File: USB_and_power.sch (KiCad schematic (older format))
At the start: 38 parts

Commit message: Updated with the ttl output
Adding a lot of footprints and other bits.
Changed TVS on USB
Added fuse on USB 5V
TTL level translators, 2x. Go from 3v3 to 1v8, then "anything" to 1v8
for the output.
2x LDO for 3v3->1v8, 3v3->2v5
Plus allow external input.
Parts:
- removed D? (x2): D_TVS, symbol Device:D_TVS
- added D1: RClamp0582BQ, Package_TO_SOT_SMD:SOT-416, symbol Power_Protection:SP0502BAJT
- added F1: 0ZCJ0075AF2E, Resistor_SMD:R_1206_3216Metric_Pad1.30x1.75mm_HandSolder, symbol Device:Polyfuse_Small
- C1, C10, C11, C12, C13, C14, C15, C16, C17, C18, C4, C5, C6, C7, C8, C9: renamed from C?; footprint (none) -> Capacitor_SMD:C_0603_1608Metric_Pad1.08x0.95mm_HandSolder
- C2: renamed from C?; footprint (none) -> Capacitor_Tantalum_SMD:CP_EIA-3528-21_Kemet-B_Pad1.50x2.35mm_HandSolder
- C3: renamed from C?; footprint (none) -> Capacitor_SMD:CP_Elec_6.3x5.7
- D3: renamed from D?; value MBRS140 -> 1A 20V; footprint (none) -> Diode_SMD:D_SOD-123
- J1: renamed from J?; footprint (none) -> Connector_USB:USB_Micro-AB_Molex_47590-0001
- R1: renamed from R?; footprint (none) -> Resistor_SMD:R_0603_1608Metric_Pad0.98x0.95mm_HandSolder
- R2, R3, R4, R5, R6, R7, R8: renamed from R?; footprint (none) -> Connector_PinHeader_2.00mm:PinHeader_1x02_P2.00mm_Vertical_SMD_Pin1Left
- U2: renamed from U?; footprint (none) -> Package_SO:SO-8_3.9x4.9mm_P1.27mm
- U3: renamed from U?; footprint (none) -> Package_QFP:LQFP-64_10x10mm_P0.5mm
- Y1: renamed from Y?; footprint (none) -> Crystal:Crystal_SMD_HC49-SD_HandSoldering
- gave numbers to parts that had none: 5
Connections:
- wire segments 213 -> 215
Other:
- note added: "750mA Bel Fuse"

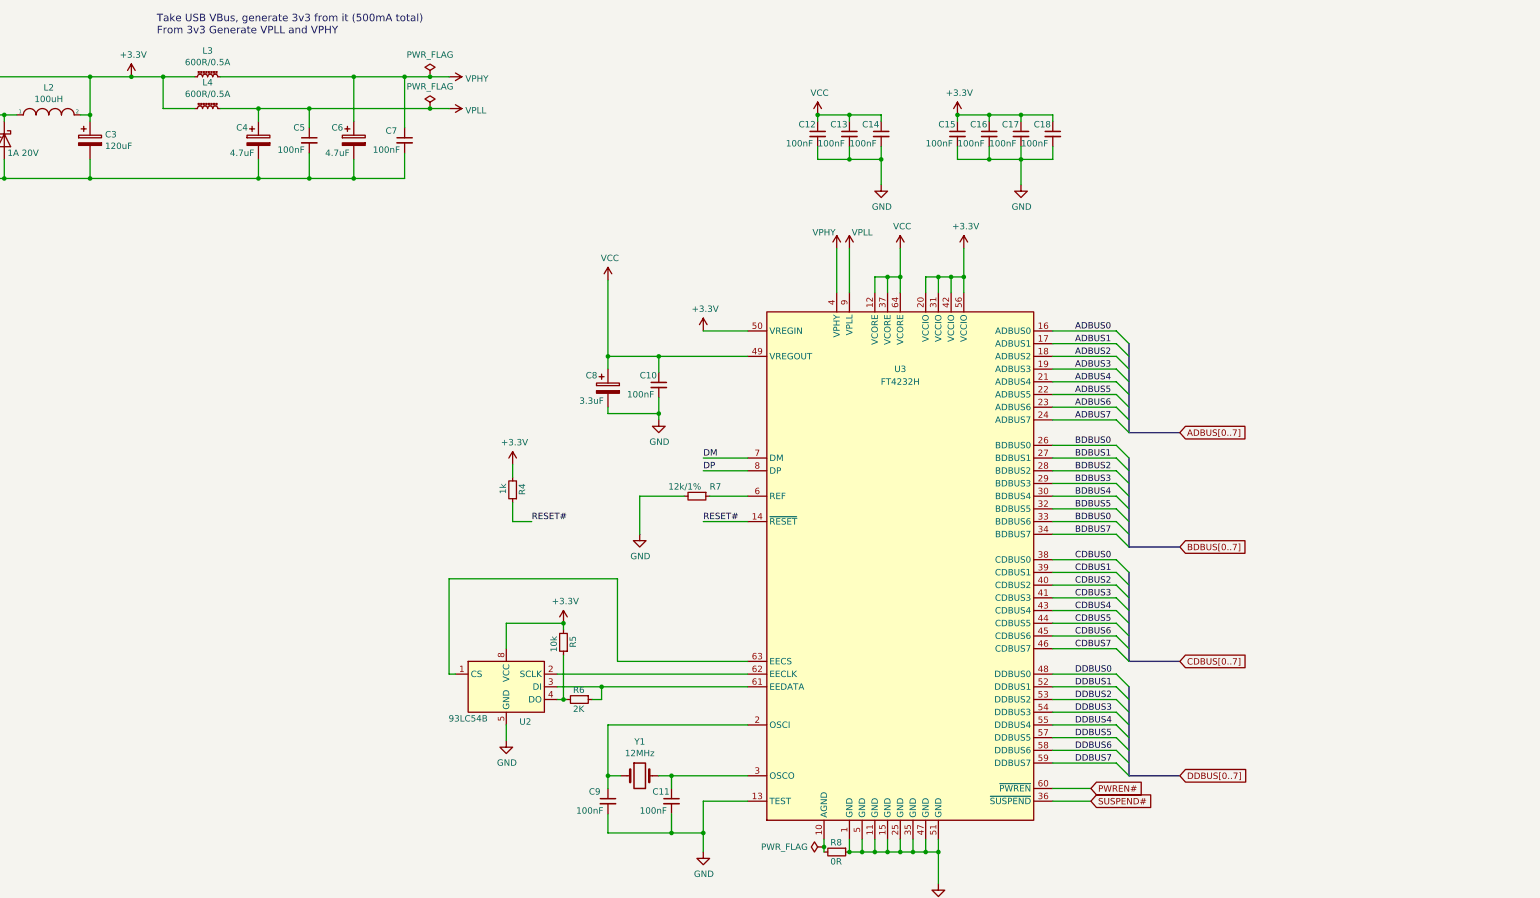
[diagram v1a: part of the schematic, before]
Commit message: Adding some LED stuff.
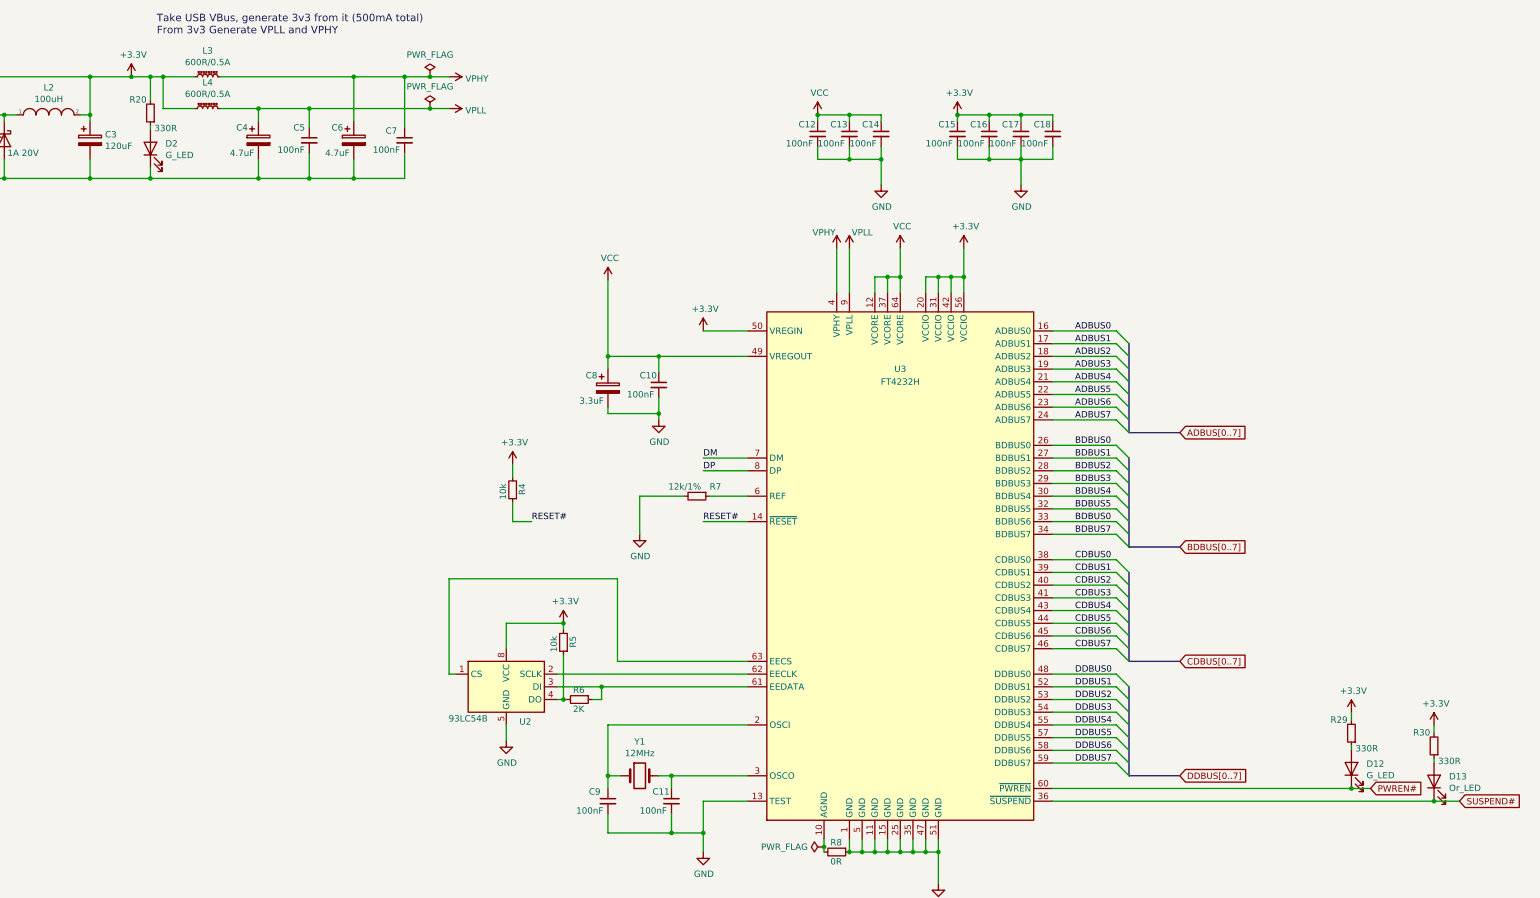
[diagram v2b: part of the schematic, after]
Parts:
- added D12, D2: G_LED, LED_SMD:LED_0603_1608Metric_Pad1.05x0.95mm_HandSolder, symbol Device:LED
- added D13: Or_LED, LED_SMD:LED_0603_1608Metric_Pad1.05x0.95mm_HandSolder, symbol Device:LED
- added R20, R29, R30: 330R, Resistor_SMD:R_0603_1608Metric_Pad0.98x0.95mm_HandSolder, symbol Device:R_Small
- R2, R3, R5, R6, R7, R8: footprint Connector_PinHeader_2.00mm:PinHeader_1x02_P2.00mm_Vertical_SMD_Pin1Left -> Resistor_SMD:R_0603_1608Metric_Pad0.98x0.95mm_HandSolder
- R4: value 1k -> 10k; footprint Connector_PinHeader_2.00mm:PinHeader_1x02_P2.00mm_Vertical_SMD_Pin1Left -> Resistor_SMD:R_0603_1608Metric_Pad0.98x0.95mm_HandSolder
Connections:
- net +3V3: now also R20.2, R29.2, R30.2
- net GND: now also D2.1 (K)
- net PWREN#: now also D12.1 (K)
- net SUSPEND#: now also D13.1 (K)
- new net: D2.2 (A), R20.1
- new net: D13.2 (A), R30.1
- new net: D12.2 (A), R29.1
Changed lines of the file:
@@
 F 0 "R2" V 3025 4900 50  0000 L CNN
 F 1 "10R" V 3025 4575 50  0000 L CNN
-F 2 "Connector_PinHeader_2.00mm:PinHeader_1x02_P2.00mm_Vertical_SMD_Pin1Left" H 3100 4800 50  0001 C CNN
+F 2 "Resistor_SMD:R_0603_1608Metric_Pad0.98x0.95mm_HandSolder" H 3100 4800 50  0001 C CNN
 F 3 "~" H 3100 4800 50  0001 C CNN
 	1    3100 4800
@@
 F 0 "R3" V 3175 5000 50  0000 L CNN
 F 1 "R10" V 3175 4675 50  0000 L CNN
-F 2 "Connector_PinHeader_2.00mm:PinHeader_1x02_P2.00mm_Vertical_SMD_Pin1Left" H 3100 4900 50  0001 C CNN
+F 2 "Resistor_SMD:R_0603_1608Metric_Pad0.98x0.95mm_HandSolder" H 3100 4900 50  0001 C CNN
 F 3 "~" H 3100 4900 50  0001 C CNN
 	1    3100 4900
@@
 	5250 3150 5500 3150
 Wire Wire Line
-	5250 3150 5000 3150
+	5250 3150 5150 3150
 Connection ~ 5000 3150
 Connection ~ 5250 3150
@@
 $EndComp
 Wire Wire Line
-	4675 3950 6000 3950
+	4675 3950 5150 3950
 Wire Wire Line
 	6000 3950 6000 3800
@@
 F 0 "R7" V 9375 6550 50  0000 L CNN
 F 1 "12k/1%" V 9375 6225 50  0000 L CNN
-F 2 "Connector_PinHeader_2.00mm:PinHeader_1x02_P2.00mm_Vertical_SMD_Pin1Left" H 9450 6450 50  0001 C CNN
+F 2 "Resistor_SMD:R_0603_1608Metric_Pad0.98x0.95mm_HandSolder" H 9450 6450 50  0001 C CNN
 F 3 "~" H 9450 6450 50  0001 C CNN
 	1    9450 6450
@@
 F 0 "R8" V 10475 9200 50  0000 L CNN
 F 1 "0R" V 10625 9200 50  0000 L CNN
-F 2 "Connector_PinHeader_2.00mm:PinHeader_1x02_P2.00mm_Vertical_SMD_Pin1Left" H 10550 9250 50  0001 C CNN
+F 2 "Resistor_SMD:R_0603_1608Metric_Pad0.98x0.95mm_HandSolder" H 10550 9250 50  0001 C CNN
 F 3 "~" H 10550 9250 50  0001 C CNN
 	1    10550 9250
@@
 F 0 "R6" V 8450 8000 50  0000 L CNN
 F 1 "2K" V 8600 8000 50  0000 L CNN
-F 2 "Connector_PinHeader_2.00mm:PinHeader_1x02_P2.00mm_Vertical_SMD_Pin1Left" H 8525 8050 50  0001 C CNN
+F 2 "Resistor_SMD:R_0603_1608Metric_Pad0.98x0.95mm_HandSolder" H 8525 8050 50  0001 C CNN
 F 3 "~" H 8525 8050 50  0001 C CNN
 	1    8525 8050
@@
 F 0 "R5" V 8325 7550 50  0000 L CNN
 F 1 "10k" V 8475 7550 50  0000 L CNN
-F 2 "Connector_PinHeader_2.00mm:PinHeader_1x02_P2.00mm_Vertical_SMD_Pin1Left" H 8400 7600 50  0001 C CNN
+F 2 "Resistor_SMD:R_0603_1608Metric_Pad0.98x0.95mm_HandSolder" H 8400 7600 50  0001 C CNN
 F 3 "~" H 8400 7600 50  0001 C CNN
 	1    8400 7600
@@
 P 8000 6400
 F 0 "R4" V 7925 6350 50  0000 L CNN
-F 1 "1k" V 8075 6350 50  0000 L CNN
-F 2 "Connector_PinHeader_2.00mm:PinHeader_1x02_P2.00mm_Vertical_SMD_Pin1Left" H 8000 6400 50  0001 C CNN
+F 1 "10k" V 8075 6350 50  0000 L CNN
+F 2 "Resistor_SMD:R_0603_1608Metric_Pad0.98x0.95mm_HandSolder" H 8000 6400 50  0001 C CNN
 F 3 "~" H 8000 6400 50  0001 C CNN
 	1    8000 6400
@@
 	8000 6200 8000 6300
 Wire Wire Line
-	12250 8750 12550 8750
-Wire Wire Line
-	12250 8850 12550 8850
-Text GLabel 12550 8750 2    50   Input ~ 0
+	12250 8750 14600 8750
+Text GLabel 14750 8750 2    50   Input ~ 0
 PWREN#
-Text GLabel 12550 8850 2    50   Input ~ 0
+Text GLabel 15450 8850 2    50   Input ~ 0
 SUSPEND#
 $Comp
@@
 Wire Wire Line
 	2100 5500 2100 5400
+Text Notes 810  4175 0    50   ~ 0
+750mA Bel Fuse
+Wire Wire Line
+	5150 3565 5150 3535
+Connection ~ 5150 3150
+Wire Wire Line
+	5150 3150 5000 3150
+Wire Wire Line
+	5150 3865 5150 3950
+Connection ~ 5150 3950
+Wire Wire Line
+	5150 3950 6000 3950
+$Comp
+L Device:R_Small R20
+U 1 1 614A5B2C
+P 5150 3435
+F 0 "R20" H 5180 3330 50  0000 L CNN
+F 1 "330R" H 4940 3555 50  0000 L CNN
+F 2 "Resistor_SMD:R_0603_1608Metric_Pad0.98x0.95mm_HandSolder" H 5150 3435 50  0001 C CNN
+F 3 "~" H 5150 3435 50  0001 C CNN
+	1    5150 3435
+	-1   0    0    1
+$EndComp
+Wire Wire Line
+	5150 3335 5150 3150
+$Comp
+L Device:LED D2
+U 1 1 61481FAA
+P 5150 3715
+F 0 "D2" V 5189 3597 50  0000 R CNN
+F 1 "G_LED" V 5098 3597 50  0000 R CNN
+F 2 "LED_SMD:LED_0603_1608Metric_Pad1.05x0.95mm_HandSolder" H 5150 3715 50  0001 C CNN
+F 3 "~" H 5150 3715 50  0001 C CNN
+	1    5150 3715
+	0    -1   -1   0
+$EndComp
+Wire Wire Line
+	15250 8545 15250 8515
+$Comp
+L Device:R_Small R30
+U 1 1 61840081
+P 15250 8415
+F 0 "R30" H 15280 8310 50  0000 L CNN
+F 1 "330R" H 15040 8535 50  0000 L CNN
+F 2 "Resistor_SMD:R_0603_1608Metric_Pad0.98x0.95mm_HandSolder" H 15250 8415 50  0001 C CNN
+F 3 "~" H 15250 8415 50  0001 C CNN
+	1    15250 8415
+	-1   0    0    1
+$EndComp
+$Comp
+L Device:LED D13
+U 1 1 6184008B
+P 15250 8695
+F 0 "D13" V 15289 8577 50  0000 R CNN
+F 1 "Or_LED" V 15198 8577 50  0000 R CNN
+F 2 "LED_SMD:LED_0603_1608Metric_Pad1.05x0.95mm_HandSolder" H 15250 8695 50  0001 C CNN
+F 3 "~" H 15250 8695 50  0001 C CNN
+	1    15250 8695
+	0    -1   -1   0
+$EndComp
+$Comp
+L power:+3.3V #PWR04
+U 1 1 61872E5E
+P 15250 8255
+F 0 "#PWR04" H 15250 8105 50  0001 C CNN
+F 1 "+3.3V" H 15265 8428 50  0000 C CNN
+F 2 "" H 15250 8255 50  0001 C CNN
+F 3 "" H 15250 8255 50  0001 C CNN
+	1    15250 8255
+	1    0    0    -1
+$EndComp
+Wire Wire Line
+	15250 8255 15250 8315
+Wire Wire Line
+	12250 8850 15250 8850
+Wire Wire Line
+	14600 8445 14600 8415
+$Comp
+L Device:R_Small R29
+U 1 1 618CACEF
+P 14600 8315
+F 0 "R29" H 14630 8210 50  0000 L CNN
+F 1 "330R" H 14390 8435 50  0000 L CNN
+F 2 "Resistor_SMD:R_0603_1608Metric_Pad0.98x0.95mm_HandSolder" H 14600 8315 50  0001 C CNN
+F 3 "~" H 14600 8315 50  0001 C CNN
+	1    14600 8315
+	-1   0    0    1
+$EndComp
+$Comp
+L Device:LED D12
+U 1 1 618CACF9
+P 14600 8595
+F 0 "D12" V 14639 8477 50  0000 R CNN
+F 1 "G_LED" V 14548 8477 50  0000 R CNN
+F 2 "LED_SMD:LED_0603_1608Metric_Pad1.05x0.95mm_HandSolder" H 14600 8595 50  0001 C CNN
+F 3 "~" H 14600 8595 50  0001 C CNN
+	1    14600 8595
+	0    -1   -1   0
+$EndComp
+$Comp
+L power:+3.3V #PWR03
+U 1 1 618CAD03
+P 14600 8155
+F 0 "#PWR03" H 14600 8005 50  0001 C CNN
+F 1 "+3.3V" H 14615 8328 50  0000 C CNN
+F 2 "" H 14600 8155 50  0001 C CNN
+F 3 "" H 14600 8155 50  0001 C CNN
+	1    14600 8155
+	1    0    0    -1
+$EndComp
+Wire Wire Line
+	14600 8155 14600 8215
+Wire Wire Line
+	14600 8750 14600 8745
+Connection ~ 14600 8750
+Wire Wire Line
+	14600 8750 14750 8750
+Wire Wire Line
+	15250 8850 15250 8845
 Wire Bus Line
 	12850 5250 12850 5950
@@
 Wire Bus Line
 	12850 7950 12850 8650
-Text Notes 810  4175 0    50   ~ 0
-750mA Bel Fuse
+Connection ~ 15250 8850
+Wire Wire Line
+	15250 8850 15450 8850
 $EndSCHEMATC

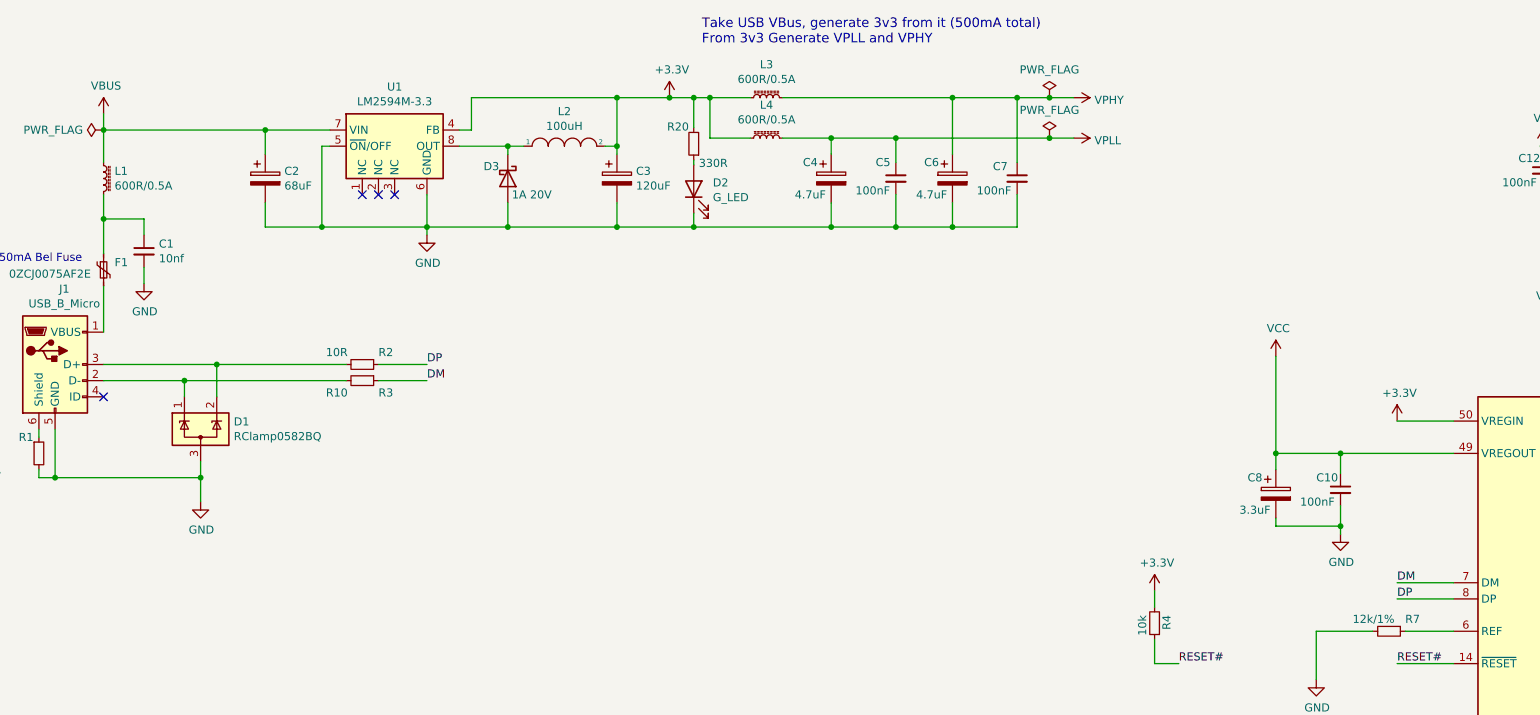
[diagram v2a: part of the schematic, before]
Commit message: Added some footprints and started to look at layout
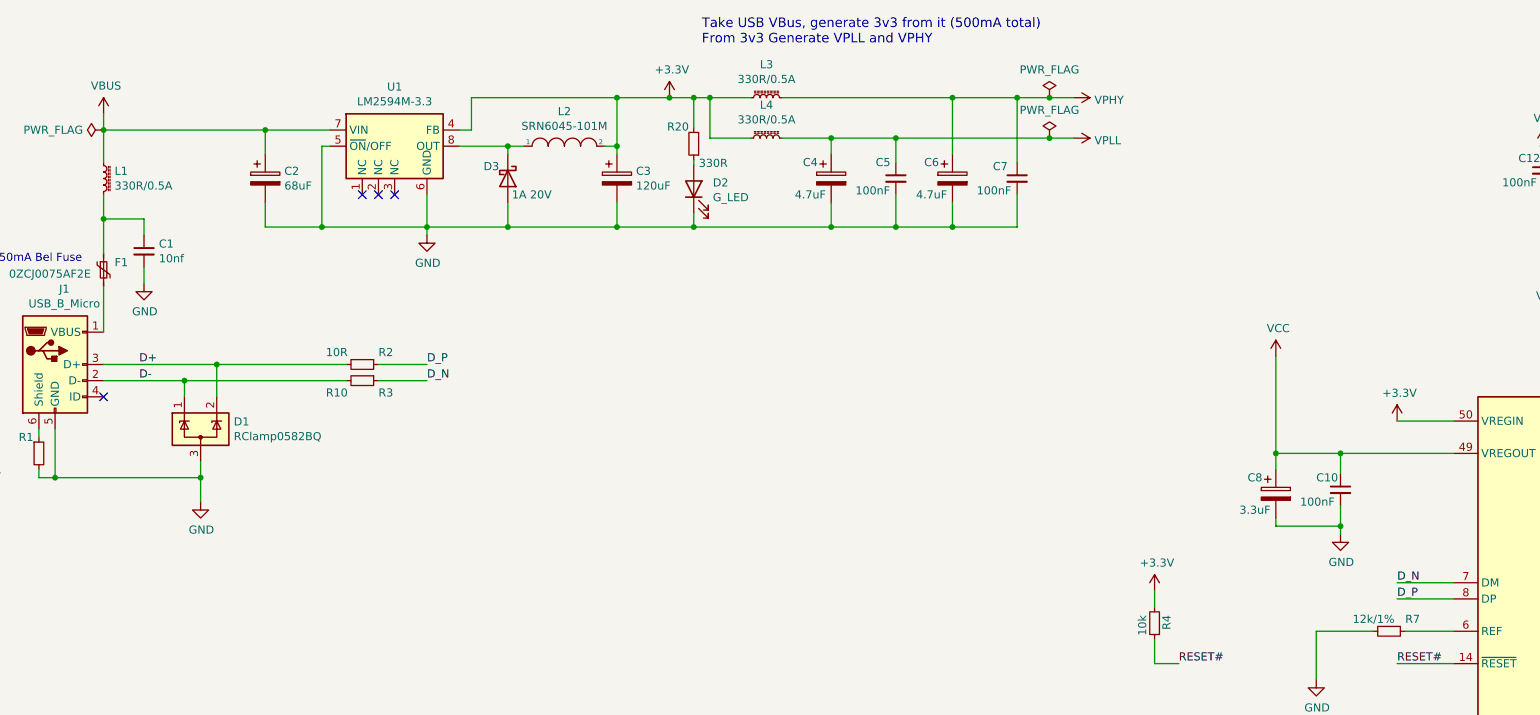
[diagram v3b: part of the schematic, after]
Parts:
- L1, L3, L4: value 600R/0.5A -> 330R/0.5A; footprint (none) -> Inductor_SMD:L_0603_1608Metric_Pad1.05x0.95mm_HandSolder
- L2: value 100uH -> SRN6045-101M; footprint (none) -> Inductor_SMD:L_Bourns_SRN6045TA
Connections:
- net D-: now reaches D1.1 (K), J1.2 (D-), R3.2
- net D+: now reaches D1.2 (K), J1.3 (D+), R2.2
- net DM renamed D_N
- net DP renamed D_P
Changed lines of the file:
@@
 P 1500 3650
 F 0 "L1" H 1568 3696 50  0000 L CNN
-F 1 "600R/0.5A" H 1568 3605 50  0000 L CNN
-F 2 "" H 1500 3650 50  0001 C CNN
+F 1 "330R/0.5A" H 1568 3605 50  0000 L CNN
+F 2 "Inductor_SMD:L_0603_1608Metric_Pad1.05x0.95mm_HandSolder" H 1500 3650 50  0001 C CNN
 F 3 "~" H 1500 3650 50  0001 C CNN
 	1    1500 3650
@@
 P 4350 3450
 F 0 "L2" H 4350 3665 50  0000 C CNN
-F 1 "100uH" H 4350 3574 50  0000 C CNN
-F 2 "" H 4350 3450 50  0001 C CNN
+F 1 "SRN6045-101M" H 4350 3574 50  0000 C CNN
+F 2 "Inductor_SMD:L_Bourns_SRN6045TA" H 4350 3450 50  0001 C CNN
 F 3 "~" H 4350 3450 50  0001 C CNN
 	1    4350 3450
@@
 P 5600 3150
 F 0 "L3" V 5805 3150 50  0000 C CNN
-F 1 "600R/0.5A" V 5714 3150 50  0000 C CNN
-F 2 "" H 5600 3150 50  0001 C CNN
+F 1 "330R/0.5A" V 5714 3150 50  0000 C CNN
+F 2 "Inductor_SMD:L_0603_1608Metric_Pad1.05x0.95mm_HandSolder" H 5600 3150 50  0001 C CNN
 F 3 "~" H 5600 3150 50  0001 C CNN
 	1    5600 3150
@@
 P 5600 3400
 F 0 "L4" V 5805 3400 50  0000 C CNN
-F 1 "600R/0.5A" V 5714 3400 50  0000 C CNN
-F 2 "" H 5600 3400 50  0001 C CNN
+F 1 "330R/0.5A" V 5714 3400 50  0000 C CNN
+F 2 "Inductor_SMD:L_0603_1608Metric_Pad1.05x0.95mm_HandSolder" H 5600 3400 50  0001 C CNN
 F 3 "~" H 5600 3400 50  0001 C CNN
 	1    5600 3400
@@
 $EndComp
 Text Label 3500 4800 0    50   ~ 0
-DP
+D_P
 Text Label 3500 4900 0    50   ~ 0
-DM
+D_N
 Wire Wire Line
 	9850 6150 9500 6150
@@
 	9850 6250 9500 6250
 Text Label 9500 6150 0    50   ~ 0
-DM
+D_N
 Text Label 9500 6250 0    50   ~ 0
-DP
+D_P
 Wire Wire Line
 	8750 5350 8750 4750
@@
 Wire Wire Line
 	15250 8850 15450 8850
+Text Label 1720 4800 0    50   ~ 0
+D+
+Text Label 1720 4900 0    50   ~ 0
+D-
 $EndSCHEMATC
